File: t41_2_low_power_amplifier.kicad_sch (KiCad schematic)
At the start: 61 parts, among them J1 5-1814832-1, J2 5-1814832-1, J3 B2B-XH-A_LF__SN_, J5 Screw_Terminal_01x02, Q1 Q_NPN_BCE, Q4 Q_NPN_BCE, Q5 Q_PMOS_GSD, Q6 Q_NPN_BEC, Q7 Q_NPN_BEC, Q8 Q_NPN_BEC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

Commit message: First version complete and sent to fab.
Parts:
- removed L2: ~, Binocular_Core:BN-43-202_VERTICAL, symbol InductorTapped:InductorTapped
- added Q2: Q_NPN_BEC, Package_TO_SOT_SMD:SOT-23-3, symbol Device:Q_NPN_BEC
- added Q3: Q_PMOS_GSD, Package_TO_SOT_SMD:SOT-23-3, symbol Device:Q_PMOS_GSD
- added R14, R24, R27: 10k, Resistor_SMD:R_1206_3216Metric, symbol Device:R_Small_US
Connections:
- net 12V: now also Q3.2 (S), R27.2
- net 12V_IN_FIL: no longer C1.1, T1.4 (SC)
- net GND: now also Q2.2 (E), R14.2
- net TXRX: now also R14.1, R24.2
- new net: Q2.3 (C), Q3.1 (G), R27.1
- new net: Q2.1 (B), R24.1
- new net 12V_FINAL: C1.1, Q3.3 (D), T1.4 (SC)
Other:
- moved on the sheet: H1, H2, H3, H4

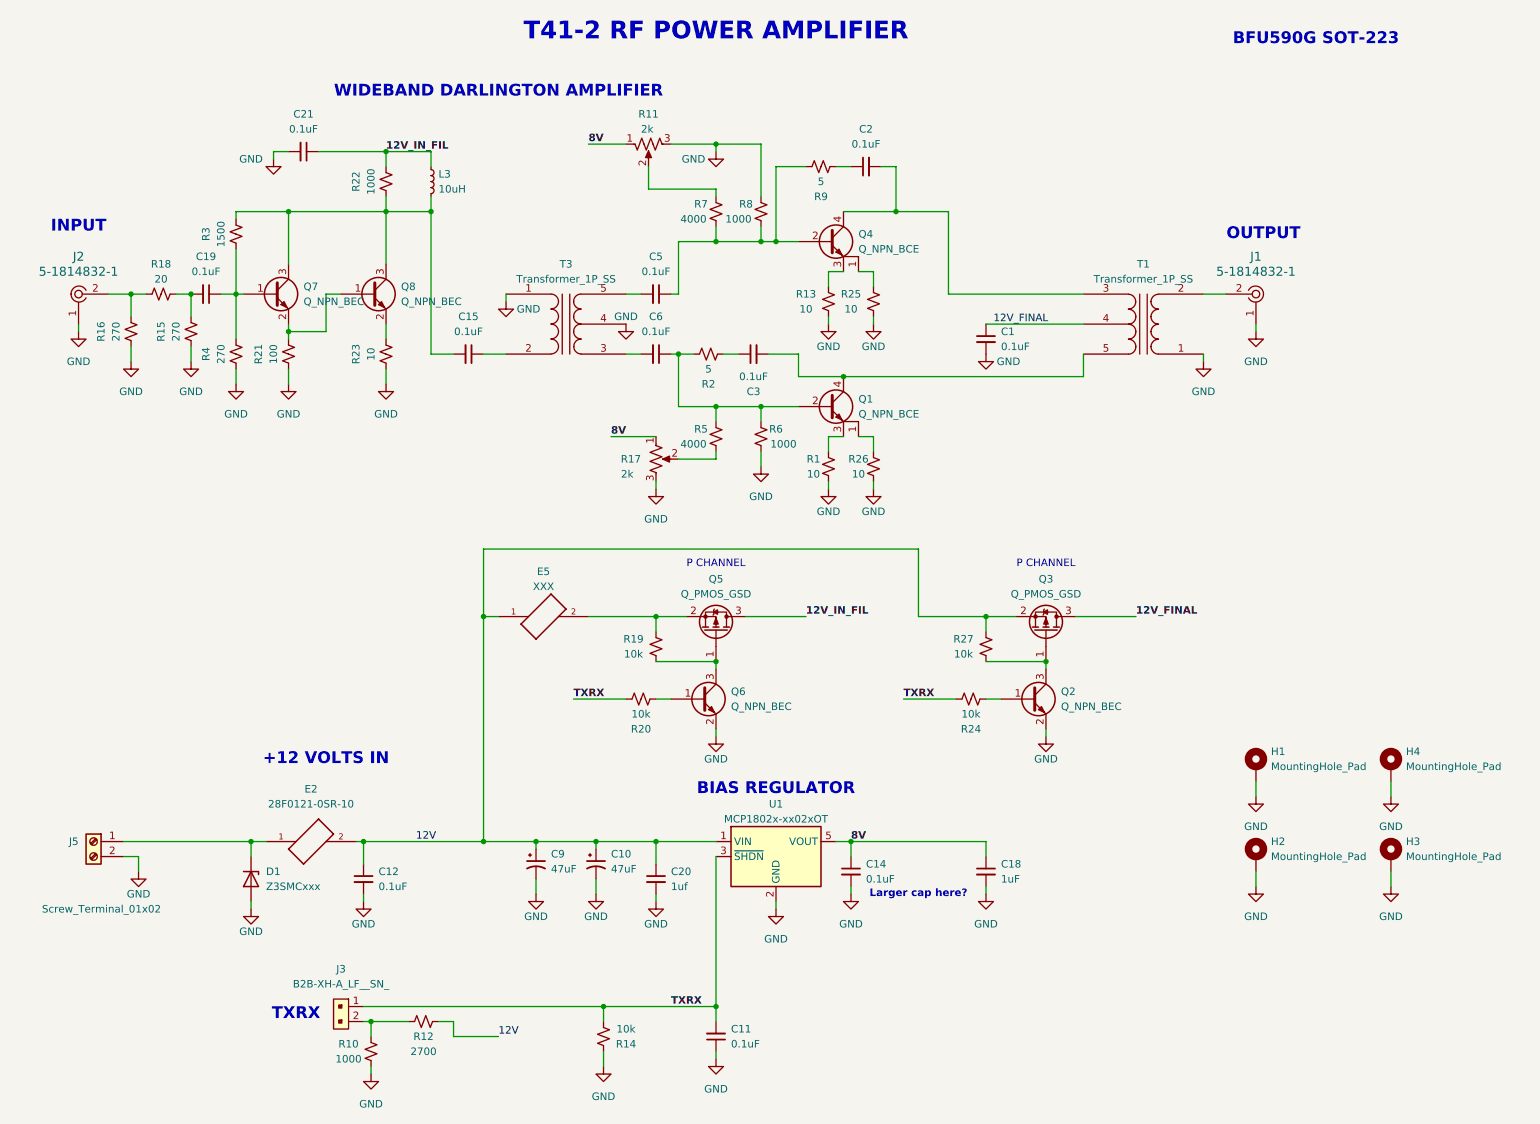
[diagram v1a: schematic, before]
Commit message: Most routing completed.
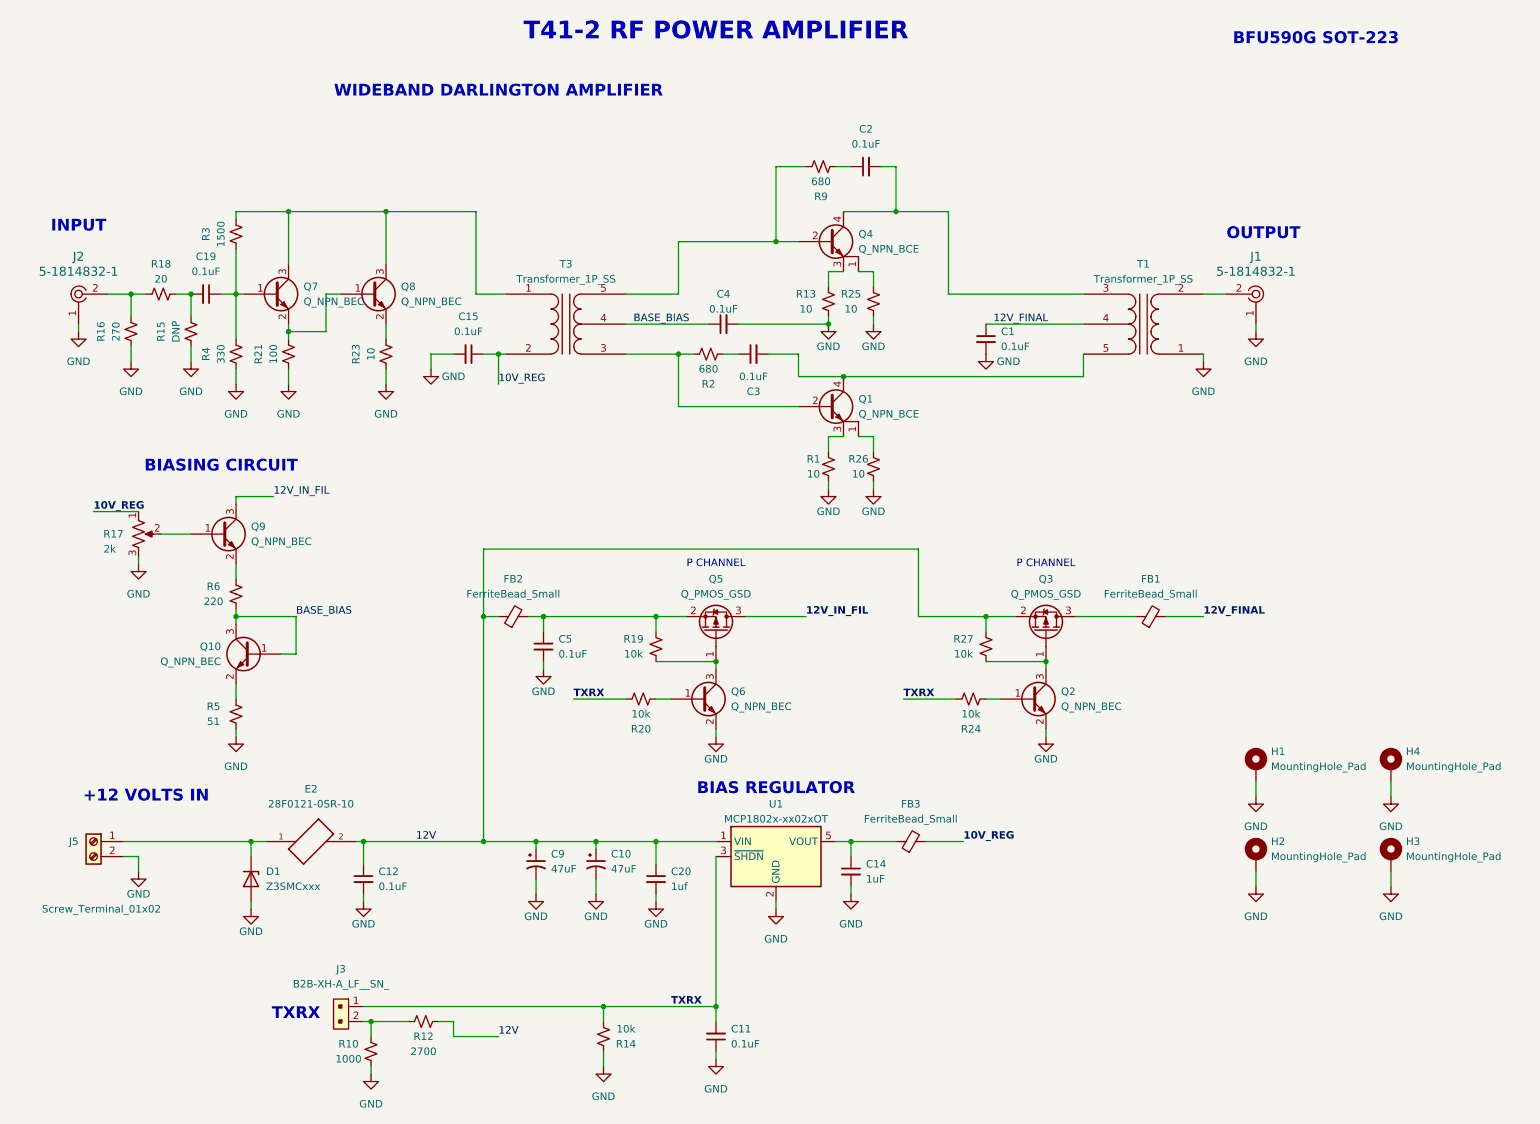
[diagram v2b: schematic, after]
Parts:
- removed C18: 1uF, Capacitor_SMD:C_1206_3216Metric, symbol Device:C_Small
- removed C21, C6: 0.1uF, Capacitor_SMD:C_1206_3216Metric, symbol Device:C_Small
- removed E5: XXX, Inductor_SMD:L_1206_3216Metric, symbol 28F0121-0SR-10:28F0121-0SR-10
- removed L3: 10uH, Inductor_SMD:L_1210_3225Metric, symbol Device:L_Small
- removed R11: 2k, Potentiometer_THT:Potentiometer_Bourns_3296W_Vertical, symbol Device:R_Potentiometer_US
- removed R22, R8: 1000, Resistor_SMD:R_1206_3216Metric, symbol Device:R_Small_US
- removed R7: 4000, Resistor_SMD:R_1206_3216Metric, symbol Device:R_Small_US
- added C4: 0.1uF, Capacitor_SMD:C_1206_3216Metric, symbol Device:C_Small
- added FB1, FB2, FB3: FerriteBead_Small, Inductor_SMD:L_1206_3216Metric, symbol Device:FerriteBead_Small
- added Q10, Q9: Q_NPN_BEC, Package_TO_SOT_SMD:SOT-23-3, symbol Device:Q_NPN_BEC
- C14: value 0.1uF -> 1uF
- R15: value 270 -> DNP
- R2, R9: value 5 -> 680
- R4: value 270 -> 330
- R5: value 4000 -> 51
- R6: value 1000 -> 220
- T1, T3: footprint Binocular_Core:BN-43-302 -> Binocular_Core:BN-43-302_Vertical
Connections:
- net 12V: now also FB2.1
- net 12V_FINAL: now also FB1.2; no longer Q3.3 (D)
- net 12V_IN_FIL: now also Q9.3 (C)
- net GND: now also C15.2, C5.2, R5.1, C4.2; no longer R6.1, T3.1 (AA), T3.4 (SC)
- net at Q7.3 (C), Q8.3 (C), R3.2: now also T3.1 (AA); no longer C15.2
- net at Q1.2 (B), R2.2: now also T3.3 (SA); no longer R5.2, R6.2
- net at R17.2: now also Q9.1 (B); no longer R5.1
- net at Q4.2 (B), R9.2: now also T3.5 (SB); no longer C5.1
- net at Q5.2 (S), R19.2: now also C5.1, FB2.2
- net 10V_REG: now reaches C15.1, T3.2 (AB)
- net 10V_REG: now also R17.1, FB3.2
- net 8V: no longer names the net of C14.1, U1.5 (VOUT)
- net 8V: now also FB3.1; no longer R17.1
- new net: Q9.2 (E), R6.2
- new net: Q10.2 (E), R5.2
- new net: FB1.1, Q3.3 (D)
- new net BASE_BIAS: C4.1, Q10.1 (B), Q10.3 (C), R6.1, T3.4 (SC)
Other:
- note added: "BIASING CIRCUIT"
- note removed: "Larger cap here?"
- moved on the sheet: R17

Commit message: Low Power Amplifier ready for fab.
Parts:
- removed C10: 47uF, Capacitor_SMD:CP_Elec_6.3x5.7, symbol Device:C_Polarized_Small_US
- added R7: 100, Resistor_SMD:R_1206_3216Metric, symbol Device:R_Small_US
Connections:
- net 12V_FINAL: now also R7.1
- net at FB1.1, Q3.3 (D): now also R7.2
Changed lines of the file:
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@@
 	)
 	(junction
-		(at 175.26 118.11)
+		(at 200.66 118.11)
 		(diameter 0)
 		(color 0 0 0 0)
 	)
 	(junction
-		(at 123.19 73.66)
+		(at 175.26 118.11)
 		(diameter 0)
 		(color 0 0 0 0)
 	)
 	(junction
-		(at 148.59 68.58)
+		(at 123.19 73.66)
 		(diameter 0)
 		(color 0 0 0 0)
 	)
 	(junction
-		(at 100.33 118.11)
+		(at 148.59 68.58)
 		(diameter 0)
 		(color 0 0 0 0)
 	)
 	(junction
-		(at 109.22 156.21)
+		(at 100.33 118.11)
 		(diameter 0)
 		(color 0 0 0 0)
@@
 	)
 	(junction
+		(at 205.74 118.11)
+		(diameter 0)
+		(color 0 0 0 0)
+	)
+	(junction
 		(at 185.42 125.73)
 		(diameter 0)
@@
 	(wire
 		(pts
-			(xy 109.22 162.56) (xy 109.22 165.1)
-		)
-		(stroke
-			(width 0)
-			(type default)
-		)
-	)
-	(wire
-		(pts
 			(xy 139.7 41.91) (xy 144.78 41.91)
 		)
@@
 	(wire
 		(pts
-			(xy 109.22 156.21) (xy 109.22 157.48)
-		)
-		(stroke
-			(width 0)
-			(type default)
-		)
-	)
-	(wire
-		(pts
 			(xy 48.26 55.88) (xy 48.26 63.5)
 		)
@@
 	(wire
 		(pts
-			(xy 99.06 156.21) (xy 109.22 156.21)
-		)
-		(stroke
-			(width 0)
-			(type default)
-		)
-	)
-	(wire
-		(pts
 			(xy 30.48 72.39) (xy 30.48 74.93)
 		)
@@
 	(wire
 		(pts
+			(xy 205.74 118.11) (xy 205.74 123.19)
+		)
+		(stroke
+			(width 0)
+			(type default)
+		)
+	)
+	(wire
+		(pts
 			(xy 149.86 41.91) (xy 152.4 41.91)
 		)
@@
 	(wire
 		(pts
-			(xy 109.22 156.21) (xy 119.38 156.21)
+			(xy 99.06 156.21) (xy 119.38 156.21)
 		)
 		(stroke
@@
 	(wire
 		(pts
+			(xy 200.66 118.11) (xy 200.66 123.19)
+		)
+		(stroke
+			(width 0)
+			(type default)
+		)
+	)
+	(wire
+		(pts
 			(xy 129.54 137.16) (xy 129.54 138.43)
 		)
@@
 	)
 	(symbol
+		(lib_id "Device:R_Small_US")
+		(at 203.2 123.19 270)
+		(unit 1)
+		(exclude_from_sim no)
+		(in_bom yes)
+		(on_board yes)
+		(dnp no)
+		(property "Reference" "R7"
+			(at 203.2 125.73 90)
+			(effects
+				(font
+					(size 1.27 1.27)
+				)
+			)
+		)
+		(property "Value" "100"
+			(at 203.2 128.27 90)
+			(effects
+				(font
+					(size 1.27 1.27)
+				)
+			)
+		)
+		(property "Footprint" "Resistor_SMD:R_1206_3216Metric"
+			(at 203.2 123.19 0)
+			(effects
+				(font
+					(size 1.27 1.27)
+				)
+				(hide yes)
+			)
+		)
+		(property "Datasheet" "~"
+			(at 203.2 123.19 0)
+			(effects
+				(font
+					(size 1.27 1.27)
+				)
+				(hide yes)
+			)
+		)
+		(property "Description" "Resistor, small US symbol"
+			(at 203.2 123.19 0)
+			(effects
+				(font
+					(size 1.27 1.27)
+				)
+				(hide yes)
+			)
+		)
+		(pin "2"
+		)
+		(pin "1"
+		)
+		(instances
+			(project "t41_2_low_power_amplifier"
+				(path "/2dfc3106-0fe9-4b2c-b32a-a54bf0a73e15"
+					(reference "R7")
+					(unit 1)
+				)
+			)
+		)
+	)
+	(symbol
 		(lib_id "power:GND")
 		(at 73.66 78.74 0)
@@
 	)
 	(symbol
-		(lib_id "power:GND")
-		(at 109.22 165.1 0)
-		(unit 1)
-		(exclude_from_sim no)
-		(in_bom yes)
-		(on_board yes)
-		(dnp no)
-		(property "Reference" "#PWR014"
-			(at 109.22 171.45 0)
-			(effects
-				(font
-					(size 1.27 1.27)
-				)
-				(hide yes)
-			)
-		)
-		(property "Value" "GND"
-			(at 109.22 168.91 0)
-			(effects
-				(font
-					(size 1.27 1.27)
-				)
-			)
-		)
-		(property "Footprint" ""
-			(at 109.22 165.1 0)
-			(effects
-				(font
-					(size 1.27 1.27)
-				)
-				(hide yes)
-			)
-		)
-		(property "Datasheet" ""
-			(at 109.22 165.1 0)
-			(effects
-				(font
-					(size 1.27 1.27)
-				)
-				(hide yes)
-			)
-		)
-		(property "Description" "Power symbol creates a global label with name \"GND\" , ground"
-			(at 109.22 165.1 0)
-			(effects
-				(font
-					(size 1.27 1.27)
-				)
-				(hide yes)
-			)
-		)
-		(pin "1"
-		)
-		(instances
-			(project "t41_2_power_amplifier"
-				(path "/2dfc3106-0fe9-4b2c-b32a-a54bf0a73e15"
-					(reference "#PWR014")
-					(unit 1)
-				)
-			)
-		)
-	)
-	(symbol
 		(lib_id "Device:FerriteBead_Small")
 		(at 95.25 118.11 90)
@@
 					(unit 1)
 				)
-			)
-		)
-	)
-	(symbol
-		(lib_id "Device:C_Polarized_Small_US")
-		(at 109.22 160.02 0)
-		(unit 1)
-		(exclude_from_sim no)
-		(in_bom yes)
-		(on_board yes)
-		(dnp no)
-		(fields_autoplaced yes)
-		(property "Reference" "C10"
-			(at 111.76 158.3181 0)
-			(effects
-				(font
-					(size 1.27 1.27)
-				)
-				(justify left)
-			)
-		)
-		(property "Value" "47uF"
-			(at 111.76 160.8581 0)
-			(effects
-				(font
-					(size 1.27 1.27)
-				)
-				(justify left)
-			)
-		)
-		(property "Footprint" "Capacitor_SMD:CP_Elec_6.3x5.7"
-			(at 109.22 160.02 0)
-			(effects
-				(font
-					(size 1.27 1.27)
-				)
-				(hide yes)
-			)
-		)
-		(property "Datasheet" "~"
-			(at 109.22 160.02 0)
-			(effects
-				(font
-					(size 1.27 1.27)
-				)
-				(hide yes)
-			)
-		)
-		(property "Description" "Polarized capacitor, small US symbol"
-			(at 109.22 160.02 0)
-			(effects
-				(font
-					(size 1.27 1.27)
-				)
-				(hide yes)
-			)
-		)
-		(pin "2"
-		)
-		(pin "1"
-		)
-		(instances
-			(project "t41_2_power_amplifier"
-				(path "/2dfc3106-0fe9-4b2c-b32a-a54bf0a73e15"
-					(reference "C10")
-					(unit 1)
-				)

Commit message: T41-2 Low Power Amplifier to fab.
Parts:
- removed Q2, Q6: Q_NPN_BEC, Package_TO_SOT_SMD:SOT-23-3, symbol Device:Q_NPN_BEC
- removed Q3, Q5: Q_PMOS_GSD, Package_TO_SOT_SMD:SOT-23-3, symbol Device:Q_PMOS_GSD
- removed R10: 1000, Resistor_SMD:R_1206_3216Metric, symbol Device:R_Small_US
- removed R12: 2700, Resistor_SMD:R_1206_3216Metric, symbol Device:R_Small_US
- removed R19, R20, R24, R27: 10k, Resistor_SMD:R_1206_3216Metric, symbol Device:R_Small_US
- removed U1: MCP1802x-xx02xOT, Package_TO_SOT_SMD:SOT-23-5, symbol Regulator_Linear:MCP1802x-xx02xOT
- added C6: 0.1uF, Capacitor_SMD:C_1206_3216Metric, symbol Device:C_Small
- added R8: 51, Resistor_SMD:R_1206_3216Metric, symbol Device:R_Small_US
- added U2: MCP1804x-C002xOT, Package_TO_SOT_SMD:SOT-23-5, symbol Regulator_Linear:MCP1804x-C002xOT
- added U3: MCP1804x-A002xOT, Package_TO_SOT_SMD:SOT-23-5, symbol Regulator_Linear:MCP1804x-A002xOT
- C11: value 0.1uF -> 0.01uF
- C14: value 1uF -> 0.1uF
- C20: value 1uf -> 0.1uF
- R23: value 10 -> 4.7
- R3: value 1500 -> 1000
- R4: value 330 -> 180
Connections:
- net 12V_IN_FIL is gone; now on net 10V_FIL: Q9.3 (C)
- net 10V_REG: no longer R17.1
- net 12V: now also U3.1 (VIN)
- net BASE_BIAS: now also R8.1; no longer Q10.1 (B), Q10.3 (C), R6.1
- net GND: now also J3.2, C6.2, U2.2 (GND), U3.2 (GND)
- net TXRX: now also U2.4 (~{SHDN}), U3.4 (~{SHDN})
- net 10V_FIL: now reaches C14.1, FB3.1
- net 10V_FIL: now also R17.1, U3.5 (VOUT)
- net 12V_REG: now reaches FB1.1, R7.2
- net 12V_REG: now also C6.1, U2.5 (VOUT)
- net at C5.1, FB2.2: now also U2.1 (VIN)
- new net: Q10.1 (B), Q10.3 (C), R6.1, R8.2
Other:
- note added: "+13.4 VOLTS IN"
- note added: "10V REGULATOR"
- note added: "12V REGULATOR"
- note added: "BFR106 SOT-23"
- note added: "BFR92P SOT-23"
- note added: "PUSH-PULL OUTPUT STAGE"
- note added: "SOT-23 MMBT5551LT1G"
- note added: "T41-2 RF LOW POWER AMPLIFIER"
- note removed: "+12 VOLTS IN"
- note removed: "BIAS REGULATOR"
- note removed: "P CHANNEL"
- note removed: "T41-2 RF POWER AMPLIFIER"
- moved on the sheet: C9, FB1, FB3, J3, R7
